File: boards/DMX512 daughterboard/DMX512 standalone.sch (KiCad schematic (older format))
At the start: 13 parts, among them J201 DB9, J202 DB9, U201 ISL83387E, U202 24AA014

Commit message: Done DMX512 daughterboard schematics
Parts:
- removed C202, C203, C204, C205, C206: 0.1u, ~, symbol CSMALL
- removed D201: LED, ~, symbol LED
- removed J201, J202: DB9, symbol DB9
- removed R201: R, ~, symbol R
- removed U201: ISL83387E, ~, symbol ISL83387E
- added P201: DMX_RX, symbol CONN_4
- added P202: DMX_TX, symbol CONN_4
- added U201: ISL8491E, ~, symbol ISL8491E
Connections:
- net labels removed: A_CTS, A_DSR, A_DTR, A_RTS, A_RX, A_TX, B_CTS, B_DSR, B_DTR, B_RTS, B_RX, B_TX, C_CTS, C_DSR, C_DTR, C_RTS, C_RX, C_TX
- wire segments 90 -> 73
- no-connect marks 4 -> 10

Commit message: Added bypass capacitor to EEPROM in DMX512 dboard
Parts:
- added C202: 0.1u, ~, symbol CSMALL
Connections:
- wire segments 73 -> 76
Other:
- moved on the sheet: R203
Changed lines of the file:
@@
 Text HLabel 4600 1500 1    60   Output ~ 0
 DSR_ISO
-Text HLabel 4700 6050 0    60   Input ~ 0
+Text HLabel 4500 6050 0    60   UnSpc ~ 0
 VCC_3V3
-Text HLabel 4550 7200 0    60   Input ~ 0
+Text HLabel 4550 7200 0    60   UnSpc ~ 0
 GND
 Text HLabel 6300 6550 2    60   BiDi ~ 0
@@
 	6300 6550 6200 6550
 Wire Wire Line
-	5300 6050 5500 6050
+	5100 6050 5500 6050
 Wire Wire Line
 	5500 6050 5500 6150
@@
 	7050 6700 7250 6700
 Wire Wire Line
-	4800 6050 4700 6050
+	4600 6050 4500 6050
 Wire Wire Line
 	2550 3550 2800 3550
@@
 L R R203
 U 1 1 53ABAC25
-P 5050 6050
-F 0 "R203" V 5130 6050 40  0000 C CNN
-F 1 "50" V 5057 6051 40  0000 C CNN
-F 2 "~" V 4980 6050 30  0000 C CNN
-F 3 "~" H 5050 6050 30  0000 C CNN
-	1    5050 6050
+P 4850 6050
+F 0 "R203" V 4930 6050 40  0000 C CNN
+F 1 "50" V 4857 6051 40  0000 C CNN
+F 2 "~" V 4780 6050 30  0000 C CNN
+F 3 "~" H 4850 6050 30  0000 C CNN
+	1    4850 6050
 	0    -1   -1   0
 $EndComp
+$Comp
+L CSMALL C202
+U 1 1 53B633ED
+P 5200 5850
+F 0 "C202" H 5225 5900 30  0000 L CNN
+F 1 "0.1u" H 5225 5800 30  0000 L CNN
+F 2 "~" H 5200 5850 60  0000 C CNN
+F 3 "~" H 5200 5850 60  0000 C CNN
+	1    5200 5850
+	1    0    0    -1
+$EndComp
+Wire Wire Line
+	5200 5950 5200 6050
+Connection ~ 5200 6050
+Text HLabel 5000 5700 0    60   UnSpc ~ 0
+GND
+Wire Wire Line
+	5000 5700 5200 5700
+Wire Wire Line
+	5200 5700 5200 5750
 $EndSCHEMATC

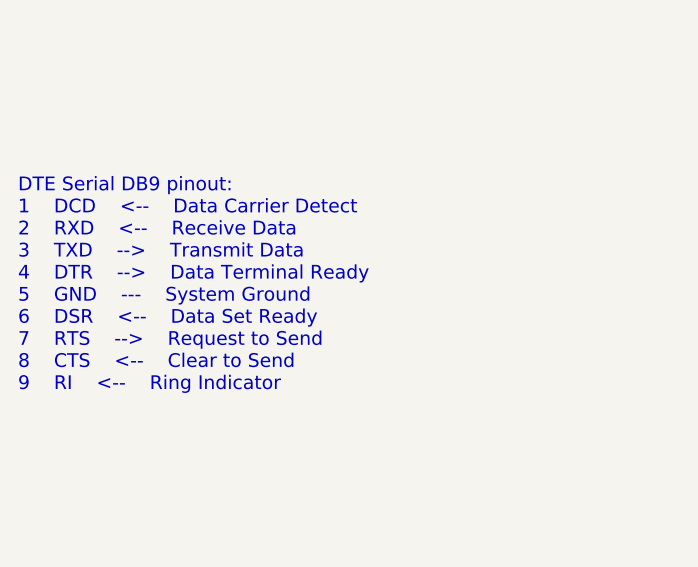
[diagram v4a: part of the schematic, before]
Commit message: Removed DB9 pinout note in DMX512 dboard
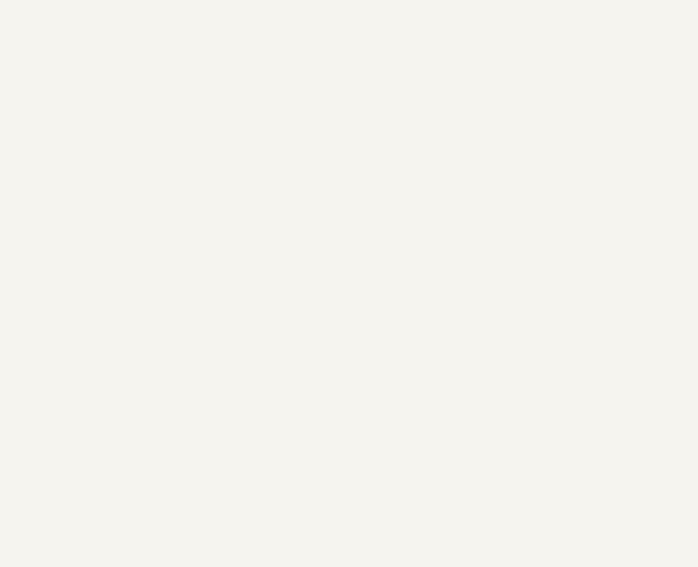
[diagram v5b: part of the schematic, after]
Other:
- note removed: "DTE Serial DB9 pinout:\n1 DCD <-- Data Carrier Detect\n2 RXD <-- Receive Data\n3 TXD --> Transmit Data\n4 DTR --> Data Terminal Ready\n5 GND --- System Ground\n6 DSR <-- Data Set Ready\n7 RTS --> Request to Send\n8 CTS <-- Clear to Send\n9 RI <-- Ring Indicator"
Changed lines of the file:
@@
 	1    0    0    -1
 $EndComp
-Text Notes 1050 6450 0    60   ~ 0
-DTE Serial DB9 pinout:\n1	DCD	<--	Data Carrier Detect\n2	RXD	<--	Receive Data\n3	TXD	-->	Transmit Data\n4	DTR	-->	Data Terminal Ready\n5	GND	---	System Ground\n6	DSR	<--	Data Set Ready\n7	RTS	-->	Request to Send\n8	CTS	<--	Clear to Send\n9	RI	<--	Ring Indicator
 $Comp
 L PWR_FLAG #FLG01
